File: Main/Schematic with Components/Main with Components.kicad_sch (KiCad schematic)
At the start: 103 parts, among them J1 USB_B_Micro, J2 XT60, J3 Conn_01x03, J4 Conn_01x03, J5 Conn_01x03, J6 Conn_01x03, J7 MSD-4-A, J9 Conn_01x03, SW1 SW_Push, SW2 SW_Push, U1 RP2350A-QFN60, U10 LM75B, U11 MCS1802GS-50-Z, U12 MCS1802GS-50-Z, U13 MCS1802GS-50-Z, U14 TPS2121RUXR, U15 AP62150WU, U2 W25Q128JVS, U3 AMS1117-3.3, U4 MMC5983MA, U5 ICM-42688-P, U6 INA226, U7 KX134-1211, U8 MS5611-01BA, U9 MCS1802GS-50-Z, Y1 ABM8-272-T3

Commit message: Resistor component numbers
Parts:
- R1: JLCPCB Part # (none) -> C2501
- R14, R15, R16, R17, R18, R21, R9: JLCPCB Part # (none) -> C25531
- R19, R20: JLCPCB Part # (none) -> C25553
- R2, R3: JLCPCB Part # (none) -> C25092
- R23, R4, R5, R6: JLCPCB Part # (none) -> C11702
- R24, R25, R26, R27: JLCPCB Part # (none) -> C25741
- R7, R8: JLCPCB Part # (none) -> C25900
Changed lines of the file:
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@@
 			)
 		)
-		(property "JLCPCB Part #" ""
+		(property "JLCPCB Part #" "C11702"
 			(at 133.35 115.57 90)
 			(effects
@@
 			)
 		)
-		(property "JLCPCB Part #" ""
+		(property "JLCPCB Part #" "C25531"
 			(at 367.03 247.65 0)
 			(effects
@@
 			)
 		)
-		(property "JLCPCB Part #" ""
+		(property "JLCPCB Part #" "C25531"
 			(at 335.28 274.32 0)
 			(effects
@@
 			)
 		)
-		(property "JLCPCB Part #" ""
+		(property "JLCPCB Part #" "C25531"
 			(at 364.49 247.65 0)
 			(effects
@@
 			)
 		)
-		(property "JLCPCB Part #" ""
+		(property "JLCPCB Part #" "C25531"
 			(at 341.63 270.51 90)
 			(effects
@@
 			)
 		)
+		(property "JLCPCB Part #" "C25741"
+			(at 494.03 201.93 0)
+			(effects
+				(font
+					(size 1.27 1.27)
+				)
+				(hide yes)
+			)
+		)
 		(pin "2"
 		)
@@
 			)
 		)
+		(property "JLCPCB Part #" "C25741"
+			(at 490.22 189.23 0)
+			(effects
+				(font
+					(size 1.27 1.27)
+				)
+				(hide yes)
+			)
+		)
 		(pin "1"
 		)
@@
 			)
 		)
-		(property "JLCPCB Part #" ""
+		(property "JLCPCB Part #" "C11702"
 			(at 53.34 110.49 90)
 			(effects
@@
 			)
 		)
+		(property "JLCPCB Part #" "C25741"
+			(at 519.43 212.09 0)
+			(effects
+				(font
+					(size 1.27 1.27)
+				)
+				(hide yes)
+			)
+		)
 		(pin "1"
 		)
@@
 			)
 		)
-		(property "JLCPCB Part #" ""
+		(property "JLCPCB Part #" "C25531"
 			(at 361.95 247.65 0)
 			(effects
@@
 			)
 		)
-		(property "JLCPCB Part #" ""
+		(property "JLCPCB Part #" "C11702"
 			(at 129.54 120.65 90)
 			(effects
@@
 			)
 		)
-		(property "JLCPCB Part #" ""
+		(property "JLCPCB Part #" "C25553"
 			(at 481.33 123.19 0)
 			(effects
@@
 			)
 		)
-		(property "JLCPCB Part #" ""
+		(property "JLCPCB Part #" "C25092"
 			(at 229.87 64.77 90)
 			(effects
@@
 			)
 		)
-		(property "JLCPCB Part #" ""
+		(property "JLCPCB Part #" "C25531"
 			(at 341.63 267.97 90)
 			(effects
@@
 			)
 		)
-		(property "JLCPCB Part #" ""
+		(property "JLCPCB Part #" "C25531"
 			(at 481.33 144.78 0)
 			(effects
@@
 			)
 		)
-		(property "JLCPCB Part #" ""
+		(property "JLCPCB Part #" "C11702"
 			(at 481.33 130.81 0)
 			(effects
@@
 			)
 		)
-		(property "JLCPCB Part #" ""
+		(property "JLCPCB Part #" "C25900"
 			(at 346.71 97.79 0)
 			(effects
@@
 			)
 		)
+		(property "JLCPCB Part #" "C25741"
+			(at 494.03 207.01 0)
+			(effects
+				(font
+					(size 1.27 1.27)
+				)
+				(hide yes)
+			)
+		)
 		(pin "1"
 		)
@@
 			)
 		)
-		(property "JLCPCB Part #" ""
+		(property "JLCPCB Part #" "C25900"
 			(at 356.87 97.79 0)
 			(effects
@@
 			)
 		)
+		(property "JLCPCB Part #" "C25553"
+			(at 490.22 184.15 0)
+			(effects
+				(font
+					(size 1.27 1.27)
+				)
+				(hide yes)
+			)
+		)
 		(pin "2"
 		)
@@
 			)
 		)
-		(property "JLCPCB Part #" ""
+		(property "JLCPCB Part #" "C25092"
 			(at 229.87 53.34 90)
 			(effects
@@
 			)
 		)
-		(property "JLCPCB Part #" ""
+		(property "JLCPCB Part #" "C2501"
 			(at 129.54 53.34 90)
 			(effects

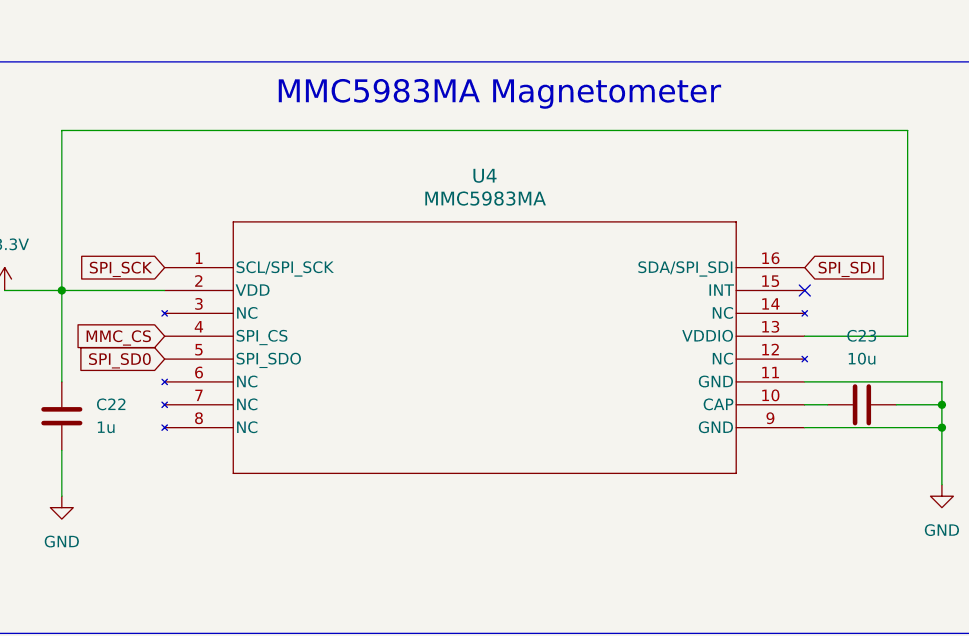
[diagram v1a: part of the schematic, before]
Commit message: Update Main with Components.kicad_sch
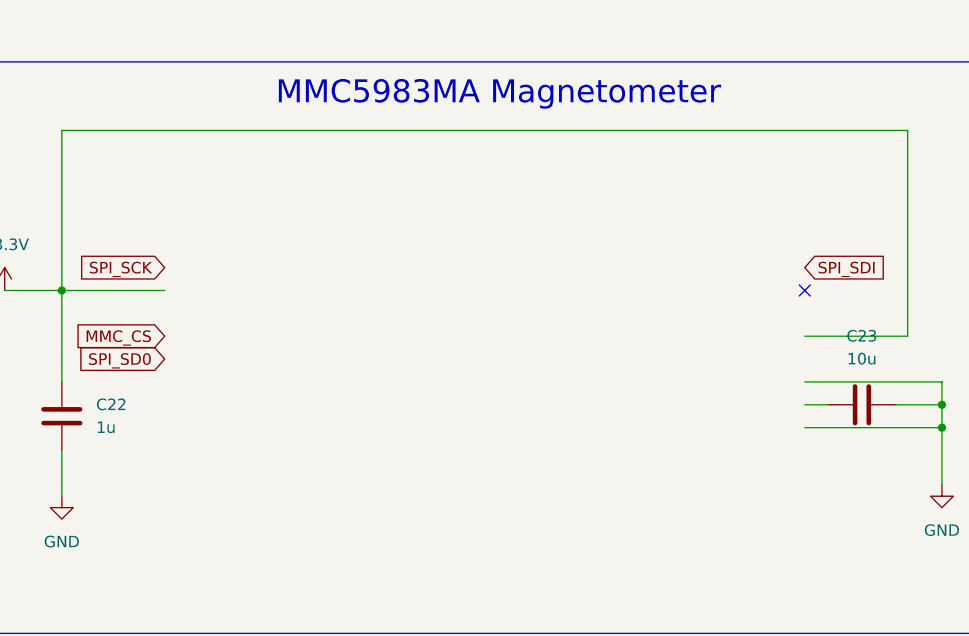
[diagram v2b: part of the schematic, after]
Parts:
- removed U4: MMC5983MA, Package_LGA:LGA-16_3x3mm_P0.5mm, symbol MMC5983MA:MMC5983MA
- D2: LCSC Part Number C84256 -> C2296
- D3: LCSC Part Number C2296 -> C2297
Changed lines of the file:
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@@
 			)
 		)
-		(property "LCSC Part Number" "C84256"
+		(property "LCSC Part Number" "C2296"
 			(at 340.36 135.89 0)
 			(effects
@@
 	)
 	(symbol
-		(lib_id "MMC5983MA:MMC5983MA")
-		(at 34.29 190.5 0)
-		(unit 1)
-		(exclude_from_sim no)
-		(in_bom yes)
-		(on_board yes)
-		(dnp no)
-		(fields_autoplaced yes)
-		(property "Reference" "U4"
-			(at 69.85 180.34 0)
-			(effects
-				(font
-					(size 1.524 1.524)
-				)
-			)
-		)
-		(property "Value" "MMC5983MA"
-			(at 69.85 182.88 0)
-			(effects
-				(font
-					(size 1.524 1.524)
-				)
-			)
-		)
-		(property "Footprint" "Package_LGA:LGA-16_3x3mm_P0.5mm"
-			(at 34.29 190.5 0)
-			(effects
-				(font
-					(size 1.27 1.27)
-					(italic yes)
-				)
-				(hide yes)
-			)
-		)
-		(property "Datasheet" "MMC5983MA"
-			(at 34.29 190.5 0)
-			(effects
-				(font
-					(size 1.27 1.27)
-					(italic yes)
-				)
-				(hide yes)
-			)
-		)
-		(property "Description" ""
-			(at 34.29 190.5 0)
-			(effects
-				(font
-					(size 1.27 1.27)
-				)
-				(hide yes)
-			)
-		)
-		(property "Availability" ""
-			(at 34.29 190.5 0)
-			(effects
-				(font
-					(size 1.27 1.27)
-				)
-				(hide yes)
-			)
-		)
-		(property "Check_prices" ""
-			(at 34.29 190.5 0)
-			(effects
-				(font
-					(size 1.27 1.27)
-				)
-				(hide yes)
-			)
-		)
-		(property "Description_1" ""
-			(at 34.29 190.5 0)
-			(effects
-				(font
-					(size 1.27 1.27)
-				)
-				(hide yes)
-			)
-		)
-		(property "MANUFACTURER" ""
-			(at 34.29 190.5 0)
-			(effects
-				(font
-					(size 1.27 1.27)
-				)
-				(hide yes)
-			)
-		)
-		(property "MAXIMUM_PACKAGE_HEIGHT" ""
-			(at 34.29 190.5 0)
-			(effects
-				(font
-					(size 1.27 1.27)
-				)
-				(hide yes)
-			)
-		)
-		(property "MF" ""
-			(at 34.29 190.5 0)
-			(effects
-				(font
-					(size 1.27 1.27)
-				)
-				(hide yes)
-			)
-		)
-		(property "MP" ""
-			(at 34.29 190.5 0)
-			(effects
-				(font
-					(size 1.27 1.27)
-				)
-				(hide yes)
-			)
-		)
-		(property "PARTREV" ""
-			(at 34.29 190.5 0)
-			(effects
-				(font
-					(size 1.27 1.27)
-				)
-				(hide yes)
-			)
-		)
-		(property "Package" ""
-			(at 34.29 190.5 0)
-			(effects
-				(font
-					(size 1.27 1.27)
-				)
-				(hide yes)
-			)
-		)
-		(property "Price" ""
-			(at 34.29 190.5 0)
-			(effects
-				(font
-					(size 1.27 1.27)
-				)
-				(hide yes)
-			)
-		)
-		(property "Purchase-URL" ""
-			(at 34.29 190.5 0)
-			(effects
-				(font
-					(size 1.27 1.27)
-				)
-				(hide yes)
-			)
-		)
-		(property "STANDARD" ""
-			(at 34.29 190.5 0)
-			(effects
-				(font
-					(size 1.27 1.27)
-				)
-				(hide yes)
-			)
-		)
-		(property "SnapEDA_Link" ""
-			(at 34.29 190.5 0)
-			(effects
-				(font
-					(size 1.27 1.27)
-				)
-				(hide yes)
-			)
-		)
-		(property "JLCPCB Part #" ""
-			(at 34.29 190.5 0)
-			(effects
-				(font
-					(size 1.27 1.27)
-				)
-				(hide yes)
-			)
-		)
-		(property "Sim.Device" ""
-			(at 34.29 190.5 0)
-			(effects
-				(font
-					(size 1.27 1.27)
-				)
-				(hide yes)
-			)
-		)
-		(pin "7"
-		)
-		(pin "8"
-		)
-		(pin "13"
-		)
-		(pin "16"
-		)
-		(pin "1"
-		)
-		(pin "4"
-		)
-		(pin "5"
-		)
-		(pin "2"
-		)
-		(pin "6"
-		)
-		(pin "15"
-		)
-		(pin "3"
-		)
-		(pin "14"
-		)
-		(pin "9"
-		)
-		(pin "12"
-		)
-		(pin "11"
-		)
-		(pin "10"
-		)
-		(instances
-			(project "Main"
-				(path "/6b66026e-3aa1-4d5a-a331-be21386153c7"
-					(reference "U4")
-					(unit 1)
-				)
-			)
-		)
-	)
-	(symbol
 		(lib_id "Device:C")
 		(at 118.11 331.47 0)
@@
 			)
 		)
-		(property "LCSC Part Number" "C2296"
+		(property "LCSC Part Number" "C2297"
 			(at 340.36 147.32 0)
 			(effects
